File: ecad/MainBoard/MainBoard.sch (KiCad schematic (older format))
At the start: 14 parts, among them IC1 RC4558, J1 ACJM-HHDR, J2 ACJM-HHDR, J3 PJ-102A, SW1 FS57003PLT2B2M2QE

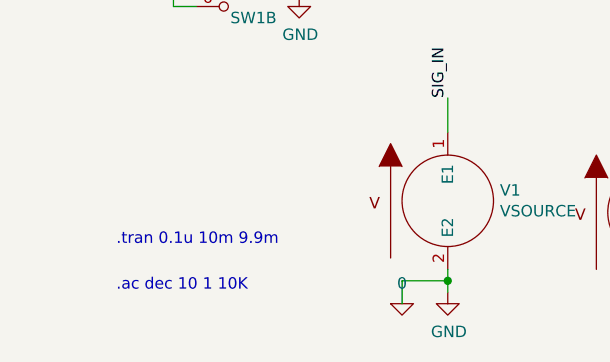
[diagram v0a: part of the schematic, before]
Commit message: Update BOM and SPIRCE SIM
Add netlist to calculate power dissipation through each resistor
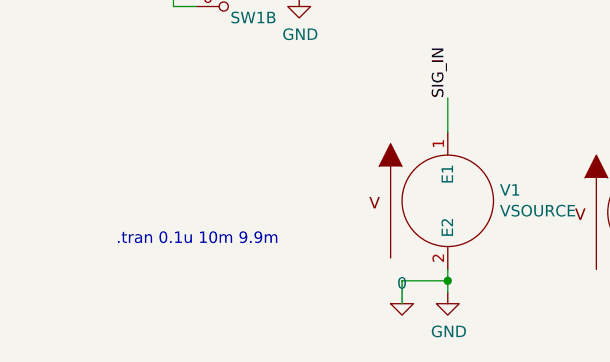
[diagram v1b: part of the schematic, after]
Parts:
- C12: MPN (none) -> LMK325ABJ107MM-T
- C7: MPN (none) -> CL31A476MPHNNNE
- D4: MPN (none) -> QBL8XX60D
- D5: Digi-Key_PN (none) -> 1N914MS-ND; MPN (none) -> 1N914
- IC1: Digi-Key_PN (none) -> 296-9650-5-ND; MPN (none) -> RC4558D
- J1, J2: Digi-Key_PN (none) -> 889-ACJM-HHDR-ND
- J3: MPN PJ-102A -> CP-102A-ND
- R10, R9: Digi-Key_PN (none) -> RG2012N-474-W-T1; MPN (none) -> RG20N470KWTR-ND
- R23: Digi-Key_PN (none) -> A130048TR-ND; MPN (none) -> CRGCQ0402J1K0
- SW1: Digi-Key_PN (none) -> EG5492-ND; MPN (none) -> FS57003PLT2B2M2QE
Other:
- note removed: ".ac dec 10 1 10K"
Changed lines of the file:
@@
 F 5 "LED" H 1600 2800 50  0001 C CNN "Spice_Model"
 F 6 "N" H 1600 2800 50  0001 C CNN "Spice_Netlist_Enabled"
+F 7 "QBL8XX60D" H 1600 2800 50  0001 C CNN "MPN"
 	1    1600 2800
 	1    0    0    -1
@@
 F 5 "1k" H 1850 2600 50  0001 C CNN "Spice_Model"
 F 6 "Y" H 1850 2600 50  0001 C CNN "Spice_Netlist_Enabled"
+F 7 "A130048TR-ND" H 1850 2600 50  0001 C CNN "Digi-Key_PN"
+F 8 "CRGCQ0402J1K0" H 1850 2600 50  0001 C CNN "MPN"
 	1    1850 2600
 	1    0    0    -1
@@
 F 3 "https://www.cui.com/product/resource/digikeypdf/pj-102a.pdf" H 950 1250 60  0001 L CNN
 F 4 "CP-102A-ND" H 950 1350 60  0001 L CNN "Digi-Key_PN"
-F 5 "PJ-102A" H 950 1450 60  0001 L CNN "MPN"
+F 5 "CP-102A-ND" H 950 1450 60  0001 L CNN "MPN"
 F 6 "Connectors, Interconnects" H 950 1550 60  0001 L CNN "Category"
 F 7 "Barrel - Power Connectors" H 950 1650 60  0001 L CNN "Family"
@@
 F 7 "Y" H 1250 950 50  0001 C CNN "Spice_Netlist_Enabled"
 F 8 "2 1" H 1250 950 50  0001 C CNN "Spice_Node_Sequence"
+F 9 "1N914MS-ND" H 1250 950 50  0001 C CNN "Digi-Key_PN"
+F 10 "1N914" H 1250 950 50  0001 C CNN "MPN"
 	1    1250 950
 	0    1    1    0
@@
 F 1 "100u" H 1450 850 50  0000 L CNN
 F 2 "Capacitor_SMD:C_0805_2012Metric_Pad1.18x1.45mm_HandSolder" H 1488 800 50  0001 C CNN
-F 3 "~" H 1450 950 50  0001 C CNN
+F 3 "https://www.yuden.co.jp/productdata/catalog/mlcc06_e.pdf" H 1450 950 50  0001 C CNN
+F 4 "LMK325ABJ107MM-T" H 1450 950 50  0001 C CNN "MPN"
 	1    1450 950
 	1    0    0    -1
@@
 F 2 "Resistor_SMD:R_0805_2012Metric_Pad1.20x1.40mm_HandSolder" V 1830 900 50  0001 C CNN
 F 3 "~" H 1900 900 50  0001 C CNN
+F 4 "RG2012N-474-W-T1" H 1900 900 50  0001 C CNN "Digi-Key_PN"
+F 5 "RG20N470KWTR-ND" H 1900 900 50  0001 C CNN "MPN"
 	1    1900 900
 	1    0    0    -1
@@
 F 2 "Resistor_SMD:R_0805_2012Metric_Pad1.20x1.40mm_HandSolder" V 1830 1300 50  0001 C CNN
 F 3 "~" H 1900 1300 50  0001 C CNN
+F 4 "RG2012N-474-W-T1" H 1900 1300 50  0001 C CNN "Digi-Key_PN"
+F 5 "RG20N470KWTR-ND" H 1900 1300 50  0001 C CNN "MPN"
 	1    1900 1300
 	1    0    0    -1
@@
 F 1 "47u" H 2318 1255 50  0000 L CNN
 F 2 "Capacitor_SMD:C_0805_2012Metric_Pad1.18x1.45mm_HandSolder" H 2238 1150 50  0001 C CNN
-F 3 "~" H 2200 1300 50  0001 C CNN
+F 3 "https://media.digikey.com/pdf/Data%20Sheets/Samsung%20PDFs/CL31A476MPHNNNE_Spec.pdf" H 2200 1300 50  0001 C CNN
+F 4 "CL31A476MPHNNNE" H 2200 1300 50  0001 C CNN "MPN"
 	1    2200 1300
 	1    0    0    -1
@@
 F 5 "ACJM-HHDR" H 6450 2250 50  0001 C CNN "Spice_Model"
 F 6 "N" H 6450 2250 50  0001 C CNN "Spice_Netlist_Enabled"
+F 7 "889-ACJM-HHDR-ND" H 6450 2250 50  0001 C CNN "Digi-Key_PN"
 	1    6450 2250
 	-1   0    0    -1
@@
 F 5 "1" H 5400 2250 50  0001 C CNN "Spice_Model"
 F 6 "N" H 5400 2250 50  0001 C CNN "Spice_Netlist_Enabled"
+F 7 "EG5492-ND" H 5400 2250 50  0001 C CNN "Digi-Key_PN"
+F 8 "FS57003PLT2B2M2QE" H 5400 2250 50  0001 C CNN "MPN"
 	3    5400 2250
 	-1   0    0    -1
@@
 F 5 "1" H 1500 2150 50  0001 C CNN "Spice_Model"
 F 6 "N" H 1500 2150 50  0001 C CNN "Spice_Netlist_Enabled"
+F 7 "EG5492-ND" H 1500 2150 50  0001 C CNN "Digi-Key_PN"
+F 8 "FS57003PLT2B2M2QE" H 1500 2150 50  0001 C CNN "MPN"
 	1    1500 2150
 	-1   0    0    -1
@@
 F 5 "1" H 1450 3000 50  0001 C CNN "Spice_Model"
 F 6 "N" H 1450 3000 50  0001 C CNN "Spice_Netlist_Enabled"
+F 7 "EG5492-ND" H 1450 3000 50  0001 C CNN "Digi-Key_PN"
+F 8 "FS57003PLT2B2M2QE" H 1450 3000 50  0001 C CNN "MPN"
 	2    1450 3000
 	-1   0    0    -1
@@
 F 5 "dc 0 ac 1 sin(200m 1 100)" H 700 2050 50  0001 C CNN "Spice_Model"
 F 6 "N" H 700 2050 50  0001 C CNN "Spice_Netlist_Enabled"
+F 7 "889-ACJM-HHDR-ND" H 700 2050 50  0001 C CNN "Digi-Key_PN"
 	1    700  2050
 	1    0    0    -1
@@
 F 6 "Y" H 2700 1150 50  0001 C CNN "Spice_Netlist_Enabled"
 F 7 "../lib/spice_models/RC4558.301.lib" H 2700 1150 50  0001 C CNN "Spice_Lib_File"
+F 8 "296-9650-5-ND" H 2700 1150 50  0001 C CNN "Digi-Key_PN"
+F 9 "RC4558D" H 2700 1150 50  0001 C CNN "MPN"
 	3    2700 1150
 	1    0    0    -1
@@
 Text Notes 900  4150 0    50   ~ 0
 .tran 0.1u 10m 9.9m
-Text Notes 900  4350 0    50   ~ 0
-.ac dec 10 1 10K
 $EndSCHEMATC

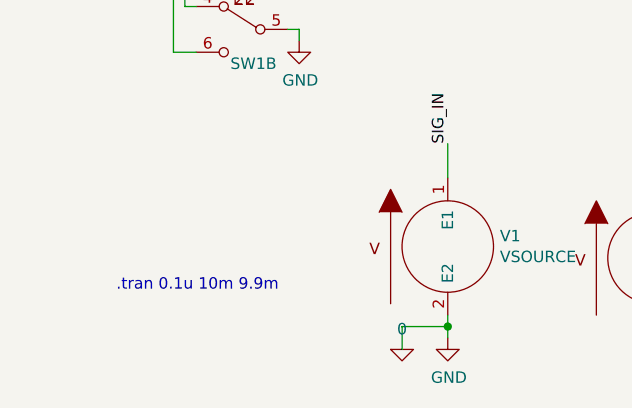
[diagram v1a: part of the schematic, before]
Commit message: Corrections + SPICE Model Finally fixed :)
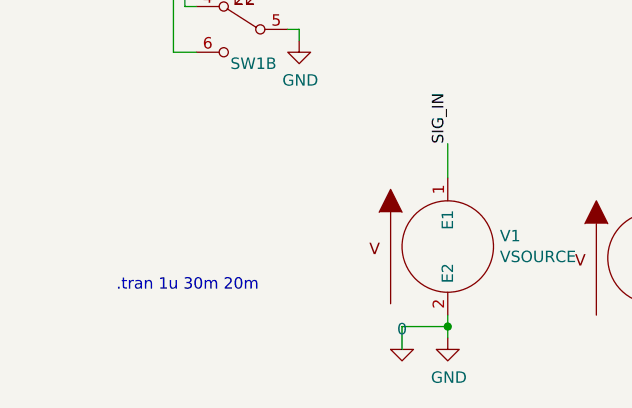
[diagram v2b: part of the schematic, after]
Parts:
- V1: Spice_Model ac 1 sin(0 150m 100k) -> ac 500m sin(0 500m 200)
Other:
- note added: ".tran 1u 30m 20m"
- note removed: ".tran 0.1u 10m 9.9m"
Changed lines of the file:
@@
 Wire Wire Line
 	2650 2150 2750 2150
-Wire Wire Line
-	3300 2150 3400 2150
 $Comp
 L pspice:VSOURCE V1
@@
 F 3 "~" H 2350 3950 50  0001 C CNN
 F 4 "V" H 2350 3950 50  0001 C CNN "Spice_Primitive"
-F 5 "ac 1 sin(0 150m 100k)" H 2350 3950 50  0001 C CNN "Spice_Model"
+F 5 "ac 500m sin(0 500m 200)" H 2350 3950 50  0001 C CNN "Spice_Model"
 F 6 "Y" H 2350 3950 50  0001 C CNN "Spice_Netlist_Enabled"
 F 7 "../lib/spice_models/audio_src.lib" H 2350 3950 50  0001 C CNN "Spice_Lib_File"
@@
 $EndComp
 Text Notes 900  4150 0    50   ~ 0
-.tran 0.1u 10m 9.9m
+.tran 1u 30m 20m
+Wire Wire Line
+	3300 2150 3400 2150
 $EndSCHEMATC

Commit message: Clean up ecad
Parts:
- C12: footprint Capacitor_SMD:C_0805_2012Metric_Pad1.18x1.45mm_HandSolder -> Capacitor_SMD:C_1210_3225Metric_Pad1.33x2.70mm_HandSolder; Digi-Key_PN (none) -> 587-6152-6-ND
- C7: footprint Capacitor_SMD:C_0805_2012Metric_Pad1.18x1.45mm_HandSolder -> Capacitor_SMD:C_1206_3216Metric_Pad1.33x1.80mm_HandSolder; Digi-Key_PN (none) -> 1276-3063-6-ND
- D4: Digi-Key_PN (none) -> 1516-1359-ND
- D5: Spice_Lib_File ../lib/spice_models/1N914.LIB -> ../lib/spice_models/1N914.lib
- IC1: footprint (none) -> DigiKey:SOIC-8_W3.9mm
- J1, J2: MPN (none) -> ACJM-HHDR
- R23: footprint Resistor_SMD:R_0805_2012Metric_Pad1.20x1.40mm_HandSolder -> Resistor_SMD:R_0402_1005Metric_Pad0.72x0.64mm_HandSolder
- V1: Spice_Lib_File ../lib/spice_models/audio_src.lib -> (none)
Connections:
- net 0: now also J2.SN, J2.TN
- no-connect marks 2 -> 0
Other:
- note added: "Power"
- note added: "SPICE Simulation"
- note added: "Signal Path"
- moved on the sheet: C12, C7, D4, D5, IC1C, J1, J2, J3, R10, R23, R9, SW1A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

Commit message: Update ecad BOM
Change transistor to 2N4424
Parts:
- C12: footprint Capacitor_SMD:C_1210_3225Metric_Pad1.33x2.70mm_HandSolder -> Capacitor_THT:CP_Radial_D10.0mm_P7.50mm; MPN LMK325ABJ107MM-T -> ECA-1VM101
- C7: footprint Capacitor_SMD:C_1206_3216Metric_Pad1.33x1.80mm_HandSolder -> Capacitor_SMD:C_0805_2012Metric_Pad1.18x1.45mm_HandSolder; MPN CL31A476MPHNNNE -> C0805C476M9PACTU
- D4: value QBL8XX60D -> LED_BLUE; MPN QBL8XX60D -> HLMP-DB25-B0000
- D5: footprint Diode_THT:D_DO-35_SOD27_P2.54mm_Vertical_AnodeUp -> Diode_THT:D_DO-35_SOD27_P7.62mm_Horizontal
- R10, R9: MPN RG20N470KWTR-ND -> ERJ-6GEYJ103V
- R23: footprint Resistor_SMD:R_0402_1005Metric_Pad0.72x0.64mm_HandSolder -> Resistor_SMD:R_0805_2012Metric_Pad1.20x1.40mm_HandSolder; MPN CRGCQ0402J1K0 -> ERA6AEB102V
- SW1: symbol screaming-panda:FS57003PLT2B2M2QE -> MainBoard-rescue:FS57003PLT2B2M2QE-screaming-panda
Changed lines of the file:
@@
 P 1650 3300
 F 0 "D4" H 1643 3517 50  0000 C CNN
-F 1 "QBL8XX60D" H 1643 3426 50  0000 C CNN
+F 1 "LED_BLUE" H 1643 3426 50  0000 C CNN
 F 2 "digikey-footprints:LED_5mm_Radial" H 1650 3300 50  0001 C CNN
-F 3 "http://www.qt-brightek.com/datasheet/QBL8XX60D.pdf" H 1650 3300 50  0001 C CNN
+F 3 "https://datasheet.octopart.com/HLMP-DB25-B0000-Broadcom-datasheet-65931945.pdf" H 1650 3300 50  0001 C CNN
 F 4 "D" H 1650 3300 50  0001 C CNN "Spice_Primitive"
 F 5 "LED" H 1650 3300 50  0001 C CNN "Spice_Model"
 F 6 "N" H 1650 3300 50  0001 C CNN "Spice_Netlist_Enabled"
-F 7 "QBL8XX60D" H 1650 3300 50  0001 C CNN "MPN"
+F 7 "HLMP-DB25-B0000" H 1650 3300 50  0001 C CNN "MPN"
 F 8 "1516-1359-ND" H 1650 3300 50  0001 C CNN "Digi-Key_PN"
 	1    1650 3300
@@
 F 0 "R23" H 2020 3146 50  0000 L CNN
 F 1 "1k" V 1950 3050 50  0000 L CNN
-F 2 "Resistor_SMD:R_0402_1005Metric_Pad0.72x0.64mm_HandSolder" V 1880 3100 50  0001 C CNN
-F 3 "https://www.te.com/commerce/DocumentDelivery/DDEController?Action=srchrtrv&DocNm=1773204-3&DocType=DS&DocLang=English" H 1950 3100 50  0001 C CNN
+F 2 "Resistor_SMD:R_0805_2012Metric_Pad1.20x1.40mm_HandSolder" V 1880 3100 50  0001 C CNN
+F 3 "https://datasheet.octopart.com/ERA6AEB102V-Panasonic-datasheet-62287448.pdf" H 1950 3100 50  0001 C CNN
 F 4 "R" H 1950 3100 50  0001 C CNN "Spice_Primitive"
 F 5 "1k" H 1950 3100 50  0001 C CNN "Spice_Model"
 F 6 "Y" H 1950 3100 50  0001 C CNN "Spice_Netlist_Enabled"
 F 7 "A130048TR-ND" H 1950 3100 50  0001 C CNN "Digi-Key_PN"
-F 8 "CRGCQ0402J1K0" H 1950 3100 50  0001 C CNN "MPN"
+F 8 "ERA6AEB102V" H 1950 3100 50  0001 C CNN "MPN"
 	1    1950 3100
 	1    0    0    -1
@@
 F 0 "D5" V 1225 1000 50  0000 L CNN
 F 1 "1N914" H 1225 900 50  0000 L CNN
-F 2 "Diode_THT:D_DO-35_SOD27_P2.54mm_Vertical_AnodeUp" H 1325 825 50  0001 C CNN
-F 3 "http://www.vishay.com/docs/85622/1n914.pdf" H 1325 1000 50  0001 C CNN
+F 2 "Diode_THT:D_DO-35_SOD27_P7.62mm_Horizontal" H 1325 825 50  0001 C CNN
+F 3 "https://datasheet.octopart.com/1N914-ON-Semiconductor-datasheet-42765246.pdf" H 1325 1000 50  0001 C CNN
 F 4 "../lib/spice_models/1N914.lib" H 1325 1000 50  0001 C CNN "Spice_Lib_File"
 F 5 "D" H 1325 1000 50  0001 C CNN "Spice_Primitive"
@@
 F 0 "C12" H 1525 1100 50  0000 L CNN
 F 1 "100u" H 1525 900 50  0000 L CNN
-F 2 "Capacitor_SMD:C_1210_3225Metric_Pad1.33x2.70mm_HandSolder" H 1563 850 50  0001 C CNN
-F 3 "https://www.yuden.co.jp/productdata/catalog/mlcc06_e.pdf" H 1525 1000 50  0001 C CNN
-F 4 "LMK325ABJ107MM-T" H 1525 1000 50  0001 C CNN "MPN"
+F 2 "Capacitor_THT:CP_Radial_D10.0mm_P7.50mm" H 1563 850 50  0001 C CNN
+F 3 "https://datasheet.octopart.com/ECA-1VM101-Panasonic-datasheet-68071800.pdf" H 1525 1000 50  0001 C CNN
+F 4 "ECA-1VM101" H 1525 1000 50  0001 C CNN "MPN"
 F 5 "587-6152-6-ND" H 1525 1000 50  0001 C CNN "Digi-Key_PN"
 	1    1525 1000
@@
 F 1 "10k" V 1975 875 50  0000 L CNN
 F 2 "Resistor_SMD:R_0805_2012Metric_Pad1.20x1.40mm_HandSolder" V 1905 950 50  0001 C CNN
-F 3 "https://www.susumu.co.jp/common/pdf/n_catalog_partition01_en.pdf" H 1975 950 50  0001 C CNN
+F 3 "https://datasheet.octopart.com/ERJ-6GEYJ103V-Panasonic-datasheet-13266872.pdf" H 1975 950 50  0001 C CNN
 F 4 "RG2012N-474-W-T1" H 1975 950 50  0001 C CNN "Digi-Key_PN"
-F 5 "RG20N470KWTR-ND" H 1975 950 50  0001 C CNN "MPN"
+F 5 "ERJ-6GEYJ103V" H 1975 950 50  0001 C CNN "MPN"
 	1    1975 950
 	1    0    0    -1
@@
 F 1 "10k" V 1975 1275 50  0000 L CNN
 F 2 "Resistor_SMD:R_0805_2012Metric_Pad1.20x1.40mm_HandSolder" V 1905 1350 50  0001 C CNN
-F 3 "https://www.susumu.co.jp/common/pdf/n_catalog_partition01_en.pdf" H 1975 1350 50  0001 C CNN
+F 3 "https://datasheet.octopart.com/ERJ-6GEYJ103V-Panasonic-datasheet-13266872.pdf" H 1975 1350 50  0001 C CNN
 F 4 "RG2012N-474-W-T1" H 1975 1350 50  0001 C CNN "Digi-Key_PN"
-F 5 "RG20N470KWTR-ND" H 1975 1350 50  0001 C CNN "MPN"
+F 5 "ERJ-6GEYJ103V" H 1975 1350 50  0001 C CNN "MPN"
 	1    1975 1350
 	1    0    0    -1
@@
 F 0 "C7" H 2443 1396 50  0000 L CNN
 F 1 "47u" H 2443 1305 50  0000 L CNN
-F 2 "Capacitor_SMD:C_1206_3216Metric_Pad1.33x1.80mm_HandSolder" H 2363 1200 50  0001 C CNN
-F 3 "https://media.digikey.com/pdf/Data%20Sheets/Samsung%20PDFs/CL31A476MPHNNNE_Spec.pdf" H 2325 1350 50  0001 C CNN
-F 4 "CL31A476MPHNNNE" H 2325 1350 50  0001 C CNN "MPN"
+F 2 "Capacitor_SMD:C_0805_2012Metric_Pad1.18x1.45mm_HandSolder" H 2363 1200 50  0001 C CNN
+F 3 "https://datasheet.octopart.com/C0805C476M9PACTU-KEMET-datasheet-149524433.pdf" H 2325 1350 50  0001 C CNN
+F 4 "C0805C476M9PACTU" H 2325 1350 50  0001 C CNN "MPN"
 F 5 "1276-3063-6-ND" H 2325 1350 50  0001 C CNN "Digi-Key_PN"
 	1    2325 1350
@@
 $EndComp
 $Comp
-L screaming-panda:FS57003PLT2B2M2QE SW1
+L MainBoard-rescue:FS57003PLT2B2M2QE-screaming-panda SW1
 U 3 1 60050ED4
 P 5450 2750
@@
 $EndComp
 $Comp
-L screaming-panda:FS57003PLT2B2M2QE SW1
+L MainBoard-rescue:FS57003PLT2B2M2QE-screaming-panda SW1
 U 1 1 60050042
 P 1550 2650
@@
 $EndComp
 $Comp
-L screaming-panda:FS57003PLT2B2M2QE SW1
+L MainBoard-rescue:FS57003PLT2B2M2QE-screaming-panda SW1
 U 2 1 600517EE
 P 1500 3500

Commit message: Library recovery
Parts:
- C12: footprint Capacitor_THT:CP_Radial_D10.0mm_P7.50mm -> screaming-panda:CAPPRD250W55D655H1220
- IC1: footprint DigiKey:SOIC-8_W3.9mm -> digikey-footprints:SOIC-8_W5.6mm

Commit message: Board 1v0
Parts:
- V1: Spice_Model ac 500m sin(0 500m 200) -> dc 1 ac 1 sin(0 1 10k)
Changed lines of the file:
@@
 F 3 "~" H 1000 4700 50  0001 C CNN
 F 4 "V" H 1000 4700 50  0001 C CNN "Spice_Primitive"
-F 5 "ac 500m sin(0 500m 200)" H 1000 4700 50  0001 C CNN "Spice_Model"
+F 5 "dc 1 ac 1 sin(0 1 10k)" H 1000 4700 50  0001 C CNN "Spice_Model"
 F 6 "Y" H 1000 4700 50  0001 C CNN "Spice_Netlist_Enabled"
-F 7 "" H 1000 4700 50  0001 C CNN "Spice_Lib_File"
 	1    1000 4700
 	1    0    0    -1

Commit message: Change to using kicad-library submodule
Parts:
- D5: Spice_Lib_File ../lib/spice_models/1N914.lib -> ../lib/kicad-library/spice_models/1N914.lib
- IC1: Spice_Lib_File ../lib/spice_models/RC4558.301.lib -> ../lib/kicad-library/spice_models/RC4558.301.lib
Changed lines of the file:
@@
 F 2 "Diode_THT:D_DO-35_SOD27_P7.62mm_Horizontal" H 1325 825 50  0001 C CNN
 F 3 "https://datasheet.octopart.com/1N914-ON-Semiconductor-datasheet-42765246.pdf" H 1325 1000 50  0001 C CNN
-F 4 "../lib/spice_models/1N914.lib" H 1325 1000 50  0001 C CNN "Spice_Lib_File"
+F 4 "../lib/kicad-library/spice_models/1N914.lib" H 1325 1000 50  0001 C CNN "Spice_Lib_File"
 F 5 "D" H 1325 1000 50  0001 C CNN "Spice_Primitive"
 F 6 "D1N914" H 1325 1000 50  0001 C CNN "Spice_Model"
@@
 F 5 "RC4558" H 2775 1150 50  0001 C CNN "Spice_Model"
 F 6 "Y" H 2775 1150 50  0001 C CNN "Spice_Netlist_Enabled"
-F 7 "../lib/spice_models/RC4558.301.lib" H 2775 1150 50  0001 C CNN "Spice_Lib_File"
+F 7 "../lib/kicad-library/spice_models/RC4558.301.lib" H 2775 1150 50  0001 C CNN "Spice_Lib_File"
 F 8 "296-9650-5-ND" H 2775 1150 50  0001 C CNN "Digi-Key_PN"
 F 9 "RC4558D" H 2775 1150 50  0001 C CNN "MPN"
